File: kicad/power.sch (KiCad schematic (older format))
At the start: 30 parts, among them CON23 PS-ON, CON24 CON6, CON25 FAN, CON26 CON5x2, Q7 FDC6401N, Q8 FDC6401N, Q9 FDC6401N

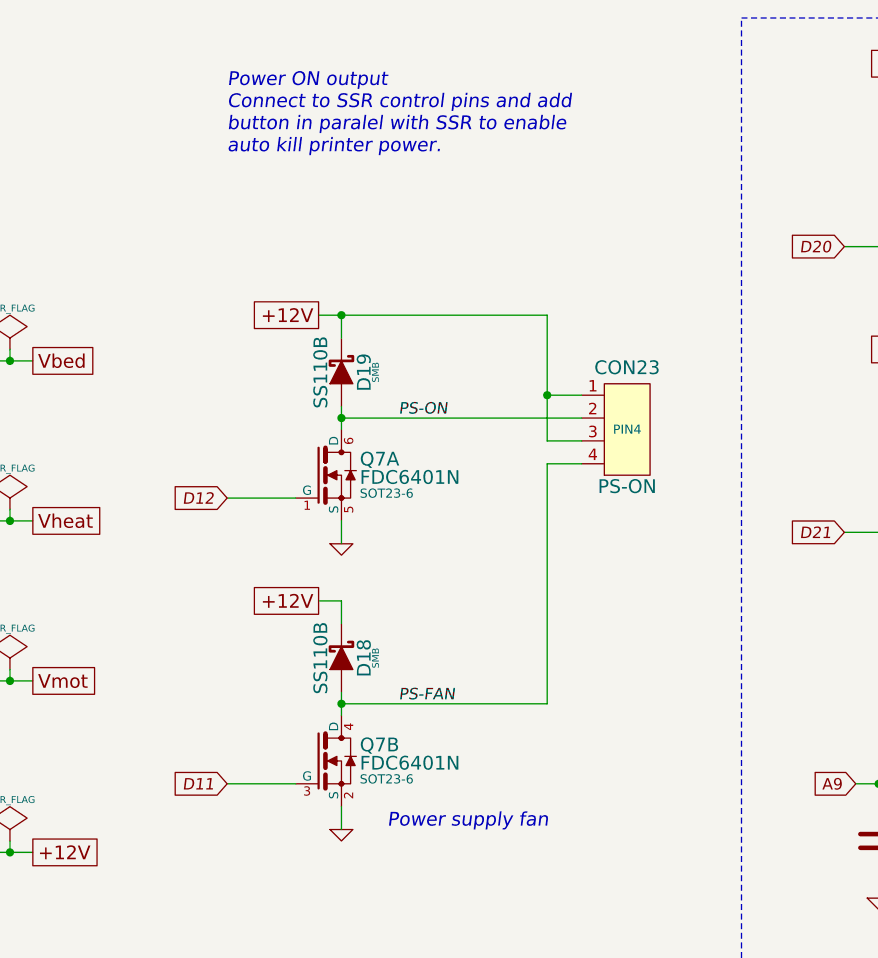
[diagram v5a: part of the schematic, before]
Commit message: Add footprint informations
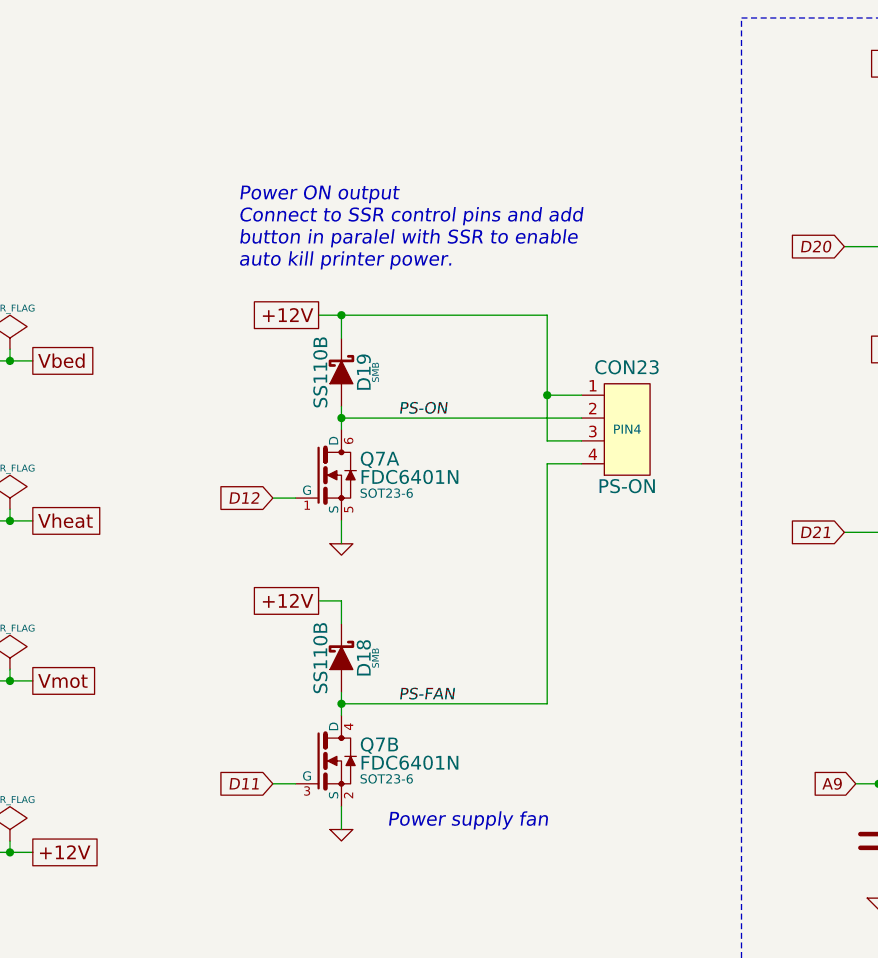
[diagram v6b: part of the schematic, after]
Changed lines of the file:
@@
 $EndDescr
 $Comp
-L GND #PWR63
+L GND #PWR056
 U 1 1 53943822
 P 1400 3250
-F 0 "#PWR63" H 1400 3250 30  0001 C CNN
+F 0 "#PWR056" H 1400 3250 30  0001 C CNN
 F 1 "GND" H 1400 3180 30  0001 C CNN
 F 2 "" H 1400 3250 60  0000 C CNN
@@
 Littelfuse MINI Blade Fuse\nmodel 0297015 (15A)\n% of rating | opening time max\n135%       | 600s\n200%       | 5 s \n350%       | 0.25 s \n600%       | 0.1 s\nReverse protection diode should \nwithstand at least 50A for 0.3s.
 $Comp
-L GND #PWR65
+L GND #PWR057
 U 1 1 53943829
 P 2900 3250
-F 0 "#PWR65" H 2900 3250 30  0001 C CNN
+F 0 "#PWR057" H 2900 3250 30  0001 C CNN
 F 1 "GND" H 2900 3180 30  0001 C CNN
 F 2 "" H 2900 3250 60  0000 C CNN
@@
 $EndComp
 $Comp
-L GND #PWR59
+L GND #PWR058
 U 1 1 5394382F
 P 2900 2550
-F 0 "#PWR59" H 2900 2550 30  0001 C CNN
+F 0 "#PWR058" H 2900 2550 30  0001 C CNN
 F 1 "GND" H 2900 2480 30  0001 C CNN
 F 2 "" H 2900 2550 60  0000 C CNN
@@
 $EndComp
 $Comp
-L GND #PWR67
+L GND #PWR059
 U 1 1 53943835
 P 2900 3950
-F 0 "#PWR67" H 2900 3950 30  0001 C CNN
+F 0 "#PWR059" H 2900 3950 30  0001 C CNN
 F 1 "GND" H 2900 3880 30  0001 C CNN
 F 2 "" H 2900 3950 60  0000 C CNN
@@
 $EndComp
 $Comp
-L GND #PWR58
+L GND #PWR060
 U 1 1 53943842
 P 1850 2550
-F 0 "#PWR58" H 1850 2550 30  0001 C CNN
+F 0 "#PWR060" H 1850 2550 30  0001 C CNN
 F 1 "GND" H 1850 2480 30  0001 C CNN
 F 2 "" H 1850 2550 60  0000 C CNN
@@
 $EndComp
 $Comp
-L GND #PWR64
+L GND #PWR061
 U 1 1 53943848
 P 1850 3250
-F 0 "#PWR64" H 1850 3250 30  0001 C CNN
+F 0 "#PWR061" H 1850 3250 30  0001 C CNN
 F 1 "GND" H 1850 3180 30  0001 C CNN
 F 2 "" H 1850 3250 60  0000 C CNN
@@
 $EndComp
 $Comp
-L GND #PWR66
+L GND #PWR062
 U 1 1 5394384E
 P 1850 3950
-F 0 "#PWR66" H 1850 3950 30  0001 C CNN
+F 0 "#PWR062" H 1850 3950 30  0001 C CNN
 F 1 "GND" H 1850 3880 30  0001 C CNN
 F 2 "" H 1850 3950 60  0000 C CNN
@@
 $EndComp
 $Comp
-L PWR_FLAG #FLG1
+L PWR_FLAG #FLG063
 U 1 1 539438AC
 P 3400 2050
-F 0 "#FLG1" H 3400 2145 30  0001 C CNN
+F 0 "#FLG063" H 3400 2145 30  0001 C CNN
 F 1 "PWR_FLAG" H 3400 2230 30  0000 C CNN
 F 2 "" H 3400 2050 60  0000 C CNN
@@
 $EndComp
 $Comp
-L PWR_FLAG #FLG2
+L PWR_FLAG #FLG064
 U 1 1 539438B2
 P 3400 2750
-F 0 "#FLG2" H 3400 2845 30  0001 C CNN
+F 0 "#FLG064" H 3400 2845 30  0001 C CNN
 F 1 "PWR_FLAG" H 3400 2930 30  0000 C CNN
 F 2 "" H 3400 2750 60  0000 C CNN
@@
 $EndComp
 $Comp
-L PWR_FLAG #FLG3
+L PWR_FLAG #FLG065
 U 1 1 539438B8
 P 3400 3450
-F 0 "#FLG3" H 3400 3545 30  0001 C CNN
+F 0 "#FLG065" H 3400 3545 30  0001 C CNN
 F 1 "PWR_FLAG" H 3400 3630 30  0000 C CNN
 F 2 "" H 3400 3450 60  0000 C CNN
@@
 $EndComp
 $Comp
-L PWR_FLAG #FLG6
+L PWR_FLAG #FLG066
 U 1 1 539438BE
 P 3400 4200
-F 0 "#FLG6" H 3400 4295 30  0001 C CNN
+F 0 "#FLG066" H 3400 4295 30  0001 C CNN
 F 1 "PWR_FLAG" H 3400 4380 30  0000 C CNN
 F 2 "" H 3400 4200 60  0000 C CNN
@@
 $EndComp
 $Comp
-L PWR_FLAG #FLG7
+L PWR_FLAG #FLG067
 U 1 1 539438C4
 P 1250 4750
-F 0 "#FLG7" H 1250 4845 30  0001 C CNN
+F 0 "#FLG067" H 1250 4845 30  0001 C CNN
 F 1 "PWR_FLAG" H 1250 4930 30  0000 C CNN
 F 2 "" H 1250 4750 60  0000 C CNN
@@
 $EndComp
 $Comp
-L GND #PWR71
+L GND #PWR068
 U 1 1 539438CA
 P 1250 4850
-F 0 "#PWR71" H 1250 4850 30  0001 C CNN
+F 0 "#PWR068" H 1250 4850 30  0001 C CNN
 F 1 "GND" H 1250 4780 30  0001 C CNN
 F 2 "" H 1250 4850 60  0000 C CNN
@@
 IOREF
 $Comp
-L PWR_FLAG #FLG5
+L PWR_FLAG #FLG069
 U 1 1 53943908
 P 1400 4150
-F 0 "#FLG5" H 1400 4245 30  0001 C CNN
+F 0 "#FLG069" H 1400 4245 30  0001 C CNN
 F 1 "PWR_FLAG" H 1400 4330 30  0000 C CNN
 F 2 "" H 1400 4150 60  0000 C CNN
@@
 $EndComp
 $Comp
-L PWR_FLAG #FLG4
+L PWR_FLAG #FLG070
 U 1 1 5394390F
 P 1100 4150
-F 0 "#FLG4" H 1100 4245 30  0001 C CNN
+F 0 "#FLG070" H 1100 4245 30  0001 C CNN
 F 1 "PWR_FLAG" H 1100 4330 30  0000 C CNN
 F 2 "" H 1100 4150 60  0000 C CNN
@@
 $EndComp
 $Comp
-L GND #PWR68
+L GND #PWR071
 U 1 1 53943ED6
 P 4850 4150
-F 0 "#PWR68" H 4850 4150 30  0001 C CNN
+F 0 "#PWR071" H 4850 4150 30  0001 C CNN
 F 1 "GND" H 4850 4080 30  0001 C CNN
 F 2 "" H 4850 4150 60  0000 C CNN
@@
 $EndComp
 $Comp
-L GND #PWR60
+L GND #PWR072
 U 1 1 53943F43
 P 4850 2900
-F 0 "#PWR60" H 4850 2900 30  0001 C CNN
+F 0 "#PWR072" H 4850 2900 30  0001 C CNN
 F 1 "GND" H 4850 2830 30  0001 C CNN
 F 2 "" H 4850 2900 60  0000 C CNN
@@
 Text GLabel 4750 1900 0    60   UnSpc ~ 0
 +12V
-Text GLabel 4350 2700 0    50   Input Italic 0
+Text GLabel 4550 2700 0    50   Input Italic 0
 D12
 Wire Wire Line
@@
 	4850 2350 5900 2350
 Wire Wire Line
-	4650 2700 4350 2700
+	4650 2700 4550 2700
 Wire Wire Line
 	4850 2900 4850 2800
@@
 Wire Wire Line
 	1400 3100 1350 3100
-Text Notes 4350 1200 0    60   Italic 0
+Text Notes 4400 1700 0    60   Italic 0
 Power ON output\nConnect to SSR control pins and add\nbutton in paralel with SSR to enable \nauto kill printer power.
 $Comp
@@
 Connection ~ 4850 3600
 Wire Wire Line
-	4650 3950 4350 3950
-Text GLabel 4350 3950 0    50   Input Italic 0
+	4650 3950 4550 3950
+Text GLabel 4550 3950 0    50   Input Italic 0
 D11
 Text Notes 5050 4150 0    60   Italic 0
@@
 D47
 $Comp
-L GND #PWR72
+L GND #PWR073
 U 1 1 53948CCE
 P 4150 6350
-F 0 "#PWR72" H 4150 6350 30  0001 C CNN
+F 0 "#PWR073" H 4150 6350 30  0001 C CNN
 F 1 "GND" H 4150 6280 30  0001 C CNN
 F 2 "" H 4150 6350 60  0000 C CNN
@@
 Connection ~ 3900 7150
 $Comp
-L GND #PWR73
+L GND #PWR074
 U 1 1 53949810
 P 3900 7200
-F 0 "#PWR73" H 3900 7200 30  0001 C CNN
+F 0 "#PWR074" H 3900 7200 30  0001 C CNN
 F 1 "GND" H 3900 7130 30  0001 C CNN
 F 2 "" H 3900 7200 60  0000 C CNN
@@
 $EndComp
 $Comp
-L GND #PWR61
+L GND #PWR075
 U 1 1 5394A1DE
 P 7550 3050
-F 0 "#PWR61" H 7550 3050 30  0001 C CNN
+F 0 "#PWR075" H 7550 3050 30  0001 C CNN
 F 1 "GND" H 7550 2980 30  0001 C CNN
 F 2 "" H 7550 3050 60  0000 C CNN
@@
 $EndComp
 $Comp
-L GND #PWR56
+L GND #PWR076
 U 1 1 5394A1E4
 P 7550 1800
-F 0 "#PWR56" H 7550 1800 30  0001 C CNN
+F 0 "#PWR076" H 7550 1800 30  0001 C CNN
 F 1 "GND" H 7550 1730 30  0001 C CNN
 F 2 "" H 7550 1800 60  0000 C CNN
@@
 Connection ~ 8500 1550
 $Comp
-L GND #PWR57
+L GND #PWR077
 U 1 1 5394B08E
 P 8500 1800
-F 0 "#PWR57" H 8500 1800 30  0001 C CNN
+F 0 "#PWR077" H 8500 1800 30  0001 C CNN
 F 1 "GND" H 8500 1730 30  0001 C CNN
 F 2 "" H 8500 1800 60  0000 C CNN
@@
 $EndComp
 $Comp
-L GND #PWR69
+L GND #PWR078
 U 1 1 5394B617
 P 7200 4450
-F 0 "#PWR69" H 7200 4450 30  0001 C CNN
+F 0 "#PWR078" H 7200 4450 30  0001 C CNN
 F 1 "GND" H 7200 4380 30  0001 C CNN
 F 2 "~" H 7200 4450 60  0000 C CNN
@@
 $EndComp
 $Comp
-L GND #PWR70
+L GND #PWR079
 U 1 1 5394B93D
 P 9050 4450
-F 0 "#PWR70" H 9050 4450 30  0001 C CNN
+F 0 "#PWR079" H 9050 4450 30  0001 C CNN
 F 1 "GND" H 9050 4380 30  0001 C CNN
 F 2 "~" H 9050 4450 60  0000 C CNN
@@
 $EndComp
 $Comp
-L GND #PWR62
+L GND #PWR080
 U 1 1 5394BA08
 P 9050 3200
-F 0 "#PWR62" H 9050 3200 30  0001 C CNN
+F 0 "#PWR080" H 9050 3200 30  0001 C CNN
 F 1 "GND" H 9050 3130 30  0001 C CNN
 F 2 "~" H 9050 3200 60  0000 C CNN

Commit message: Place components
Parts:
- CON26: value CON5x2 -> Chamber
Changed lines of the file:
@@
 P 8800 1450
 F 0 "CON26" H 8800 1770 60  0000 C CNN
-F 1 "CON5x2" H 8800 1150 60  0000 C CNN
+F 1 "Chamber" H 8800 1150 60  0000 C CNN
 F 2 "IDC10" H 8800 1450 40  0000 C CNN
 F 3 "" H 8800 1450 40  0000 C CNN
